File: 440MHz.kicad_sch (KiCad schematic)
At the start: 51 parts, among them J5 BWSMA-KWE-Z001, U10 74LVC1GU04DRL, U7 GRF5604, U9 SKYA21003

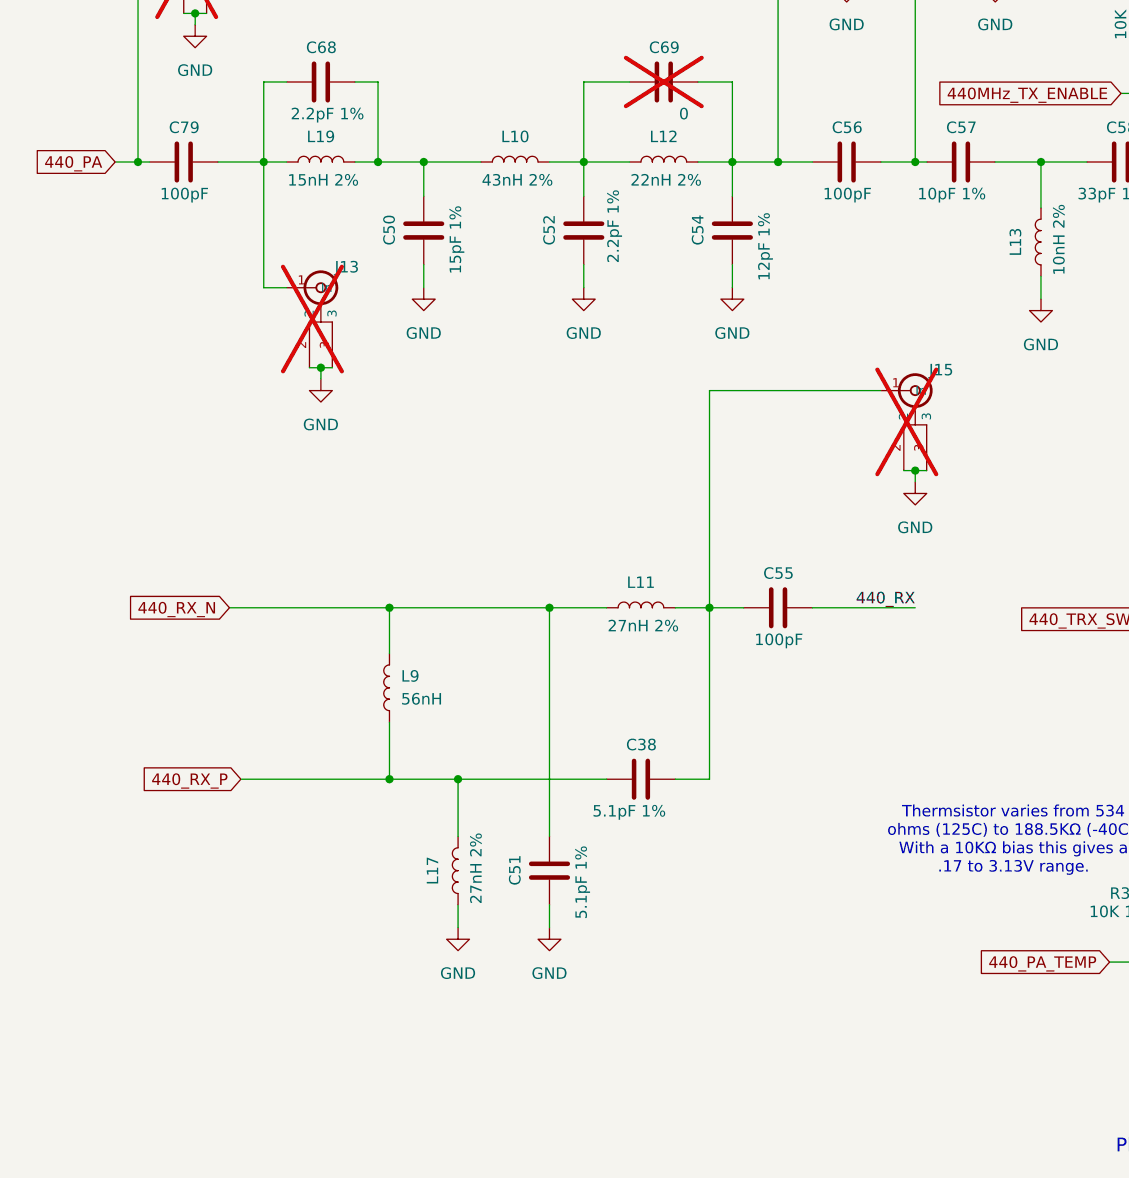
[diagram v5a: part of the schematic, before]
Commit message: Rework the cc1125 matching networks
Per combining information from the 169MHz PA design (to separate the PA
and LNA outputs) and the 440 design (to get the component values).

Signed-off-by: Corey Minyard <corey@minyard.net>
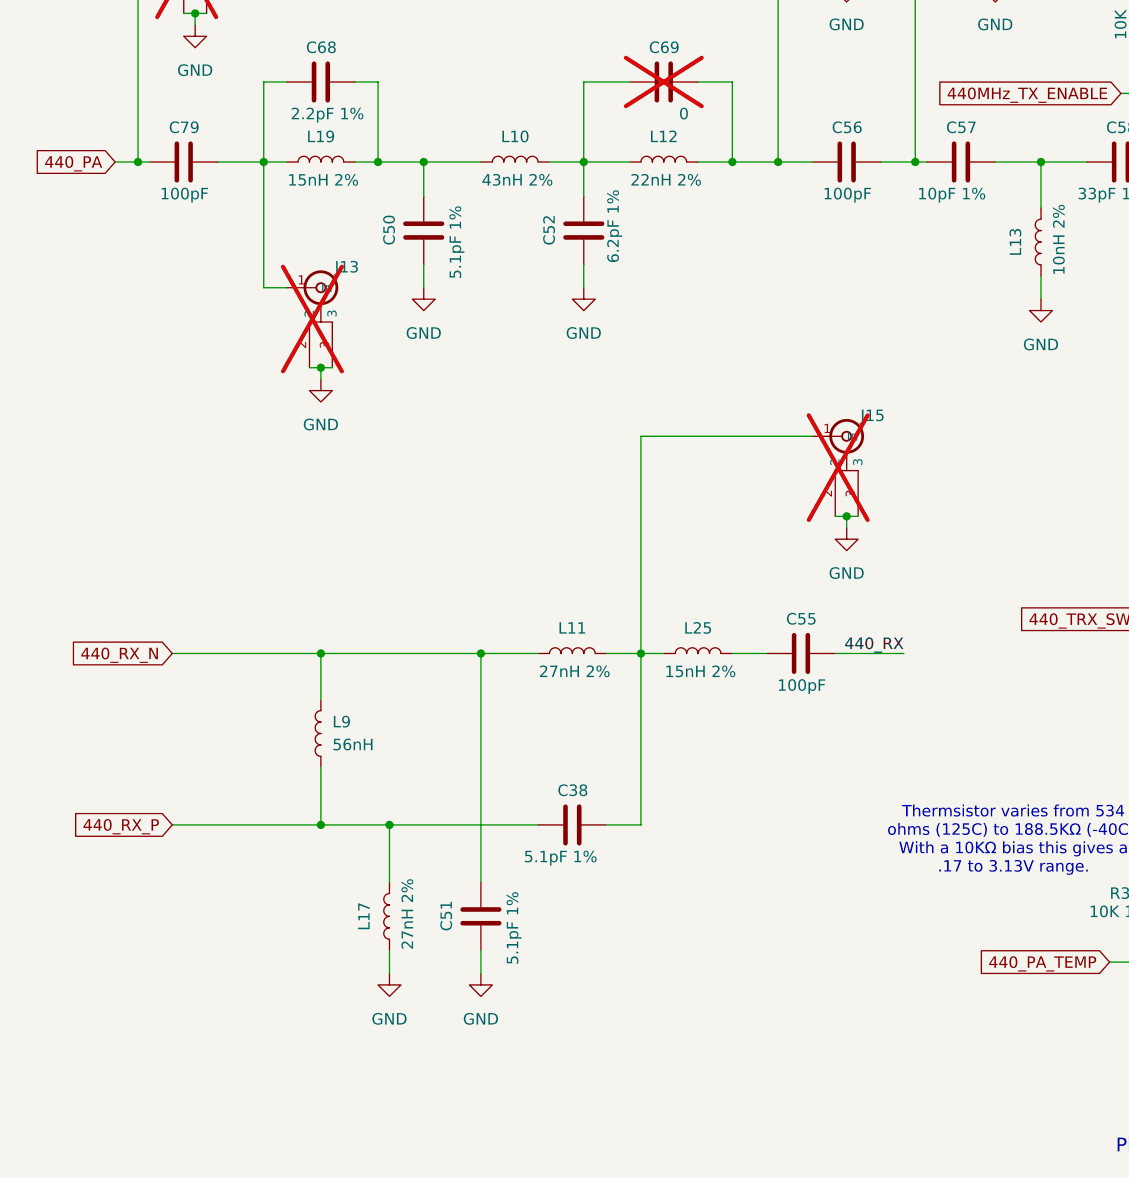
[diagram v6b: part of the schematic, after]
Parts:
- removed C54: 12pF 1%, Capacitor_SMD:C_0402_1005Metric_Pad0.74x0.62mm_HandSolder, symbol Device:C
- added L25: 15nH 2%, Inductor_SMD:L_0402_1005Metric_Pad0.77x0.64mm_HandSolder, symbol Device:L
- C50: value 15pF 1% -> 5.1pF 1%
- C52: value 2.2pF 1% -> 6.2pF 1%
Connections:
- net at C38.2, J15.1 (In), L11.2: now also L25.1; no longer C55.1
- new net: C55.1, L25.2
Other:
- moved on the sheet: C38, C51, C55, J15, L11, L17, L9

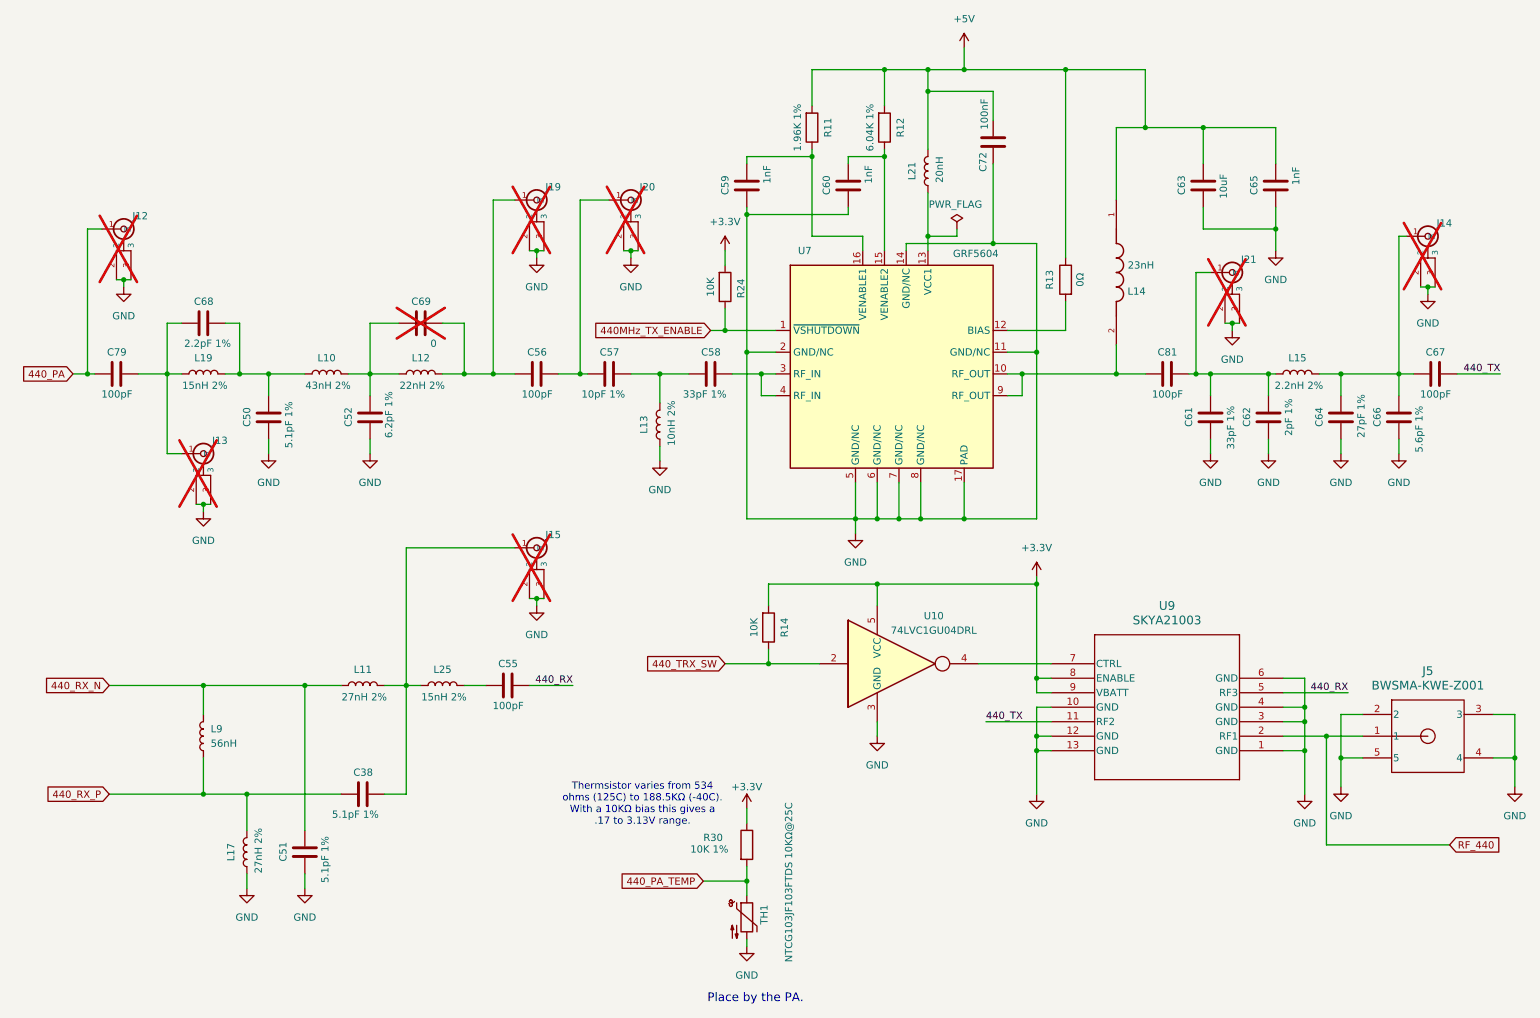
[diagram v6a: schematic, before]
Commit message: Control the 440 switch directly from the CPU
The RX/TX switch on the CC1125 added a lot of complexity with the inverter
and such.  Instead, just drive it frmo the CC1125.

Use the RX/TX switch on the CC1125 as an option shown on the design with
169MHz and an external PA, not populated.

Signed-off-by: Corey Minyard <corey@minyard.net>
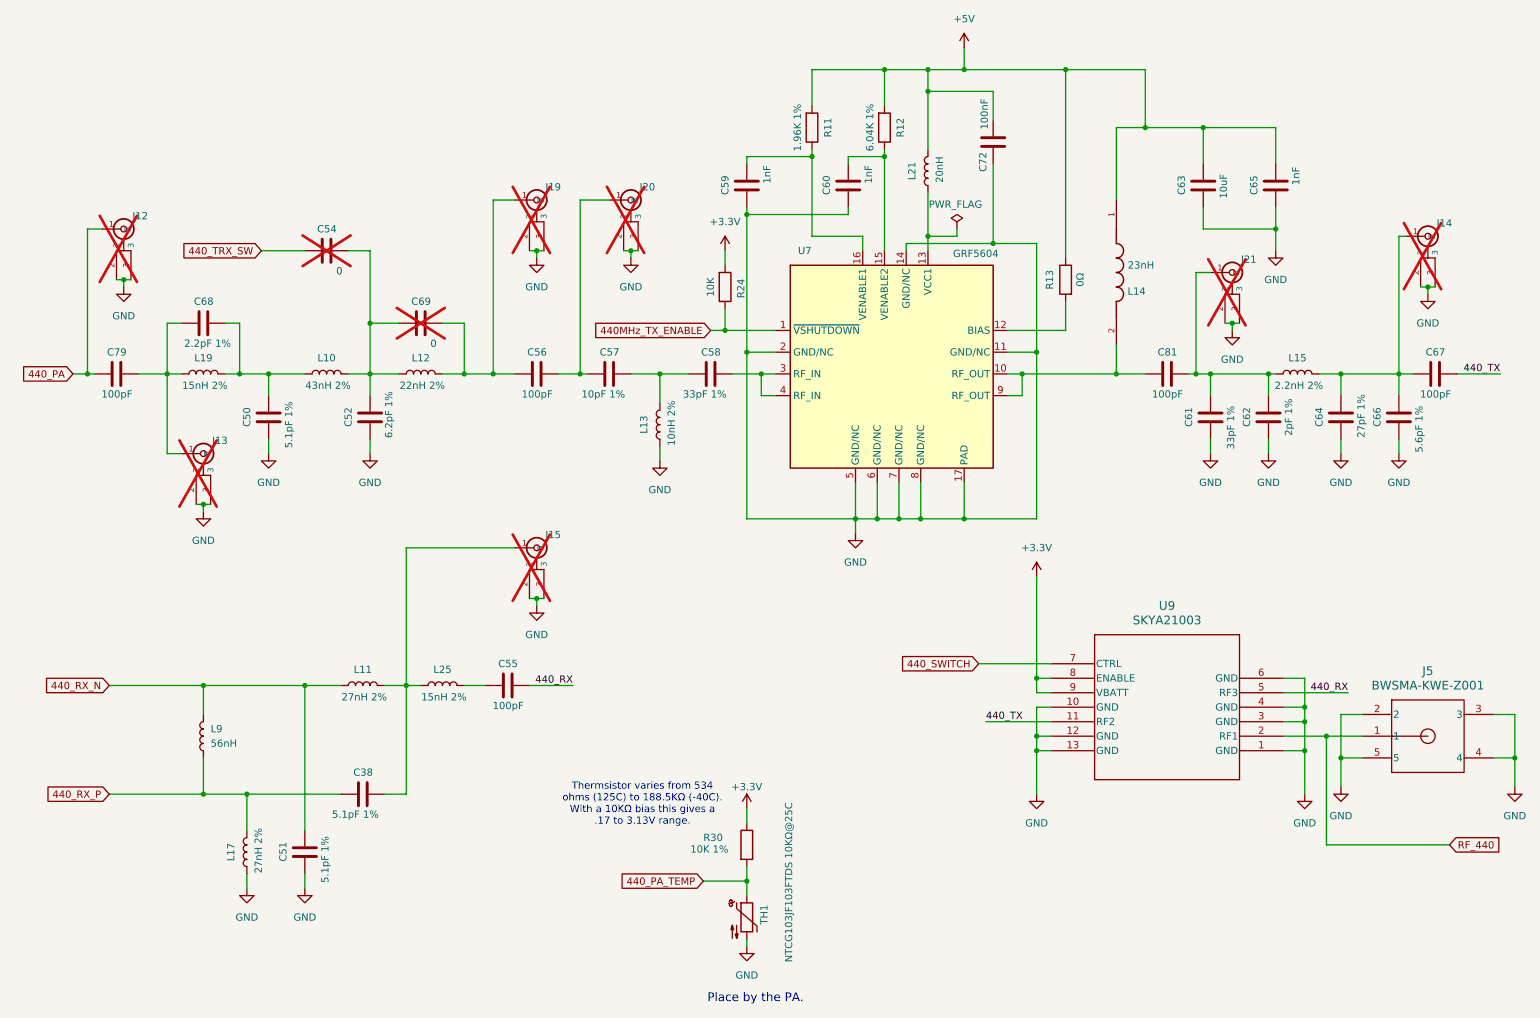
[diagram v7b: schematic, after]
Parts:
- removed R14: 10K, Resistor_SMD:R_0402_1005Metric, symbol Device:R
- removed U10: 74LVC1GU04DRL, Package_TO_SOT_SMD:SOT-553, symbol 74xGxx:74LVC1GU04DRL
- added C54: 0, Capacitor_SMD:C_0402_1005Metric_Pad0.74x0.62mm_HandSolder, symbol Device:C
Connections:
- net 440_TRX_SW: now also C54.1
- net at C52.2, C69.1, L10.2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: now also C54.2
- net 440_SWITCH: now reaches U9.7 (CTRL)

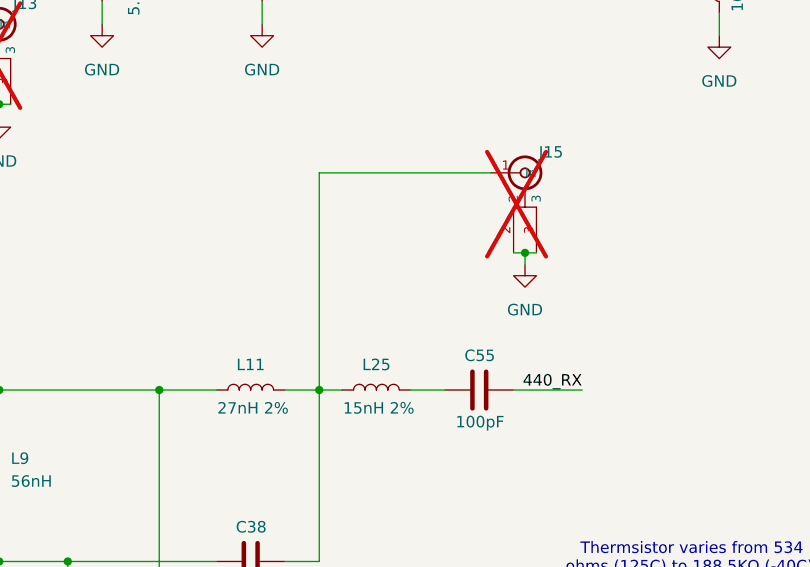
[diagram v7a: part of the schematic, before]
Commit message: Adjust the location of a U.FL test connector
Put it at the input of the 440 LNA match, it moved since an inductor was
added.

Signed-off-by: Corey Minyard <corey@minyard.net>
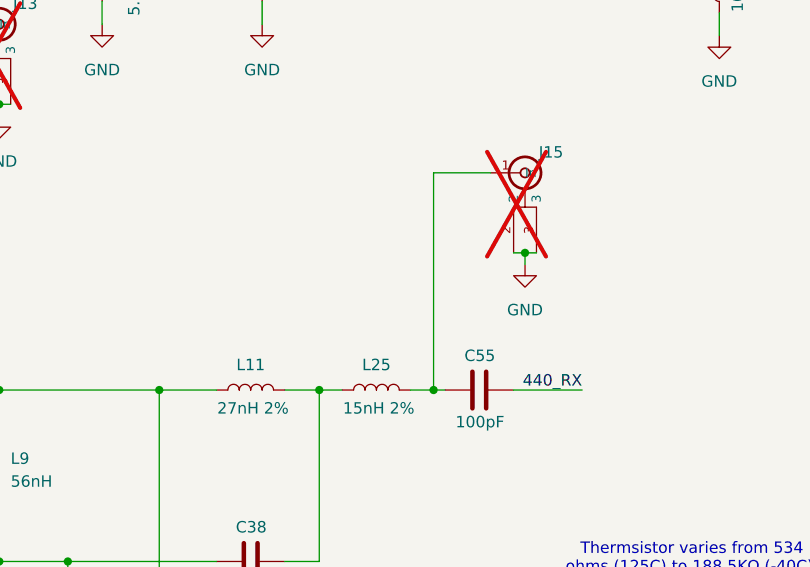
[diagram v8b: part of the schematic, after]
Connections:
- net at C38.2, L11.2, L25.1: no longer J15.1 (In)
- net at C55.1, L25.2: now also J15.1 (In)
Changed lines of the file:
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@@
+	)
+	(junction
+		(at 95.25 133.35)
+		(diameter 0)
+		(color 0 0 0 0)
 	)
 	(junction
@@
 	(wire
 		(pts
-			(xy 96.52 133.35) (xy 92.71 133.35)
+			(xy 96.52 133.35) (xy 95.25 133.35)
 		)
 		(stroke
@@
 	(wire
 		(pts
+			(xy 95.25 133.35) (xy 92.71 133.35)
+		)
+		(stroke
+			(width 0)
+			(type default)
+		)
+	)
+	(wire
+		(pts
 			(xy 165.1 104.14) (xy 168.91 104.14)
 		)
@@
 	(wire
 		(pts
+			(xy 95.25 109.22) (xy 95.25 133.35)
+		)
+		(stroke
+			(width 0)
+			(type default)
+		)
+	)
+	(wire
+		(pts
 			(xy 127 78.74) (xy 132.08 78.74)
 		)
@@
 	(wire
 		(pts
-			(xy 82.55 109.22) (xy 101.6 109.22)
+			(xy 101.6 109.22) (xy 95.25 109.22)
 		)
 		(stroke
@@
 		)
 		(stroke
-			(width 0)
-			(type default)
-		)
-	)
-	(wire
-		(pts
-			(xy 82.55 109.22) (xy 82.55 133.35)
-		)
-		(stroke
